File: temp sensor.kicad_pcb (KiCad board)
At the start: 2 copper layers, 48.2 x 24.9 mm, 52 parts, among them IC1 ESP32-C3-MINI-1, J1 USB_C_Receptacle_USB2.0, J2 Conn_01x02_Male, J3 Conn_01x06_Male, J4 USB_B_Micro, J5 Conn_01x02_Male, J6 Conn_01x02_Male, Q1 BC847BDW1, SW1 SW_Push_Right_Angle, SW2 SW_Push_Right_Angle, U1 SHTC3, U2 TLV62569DBV, U3 BME280, U4 Si7020-A20, U5 SN65220

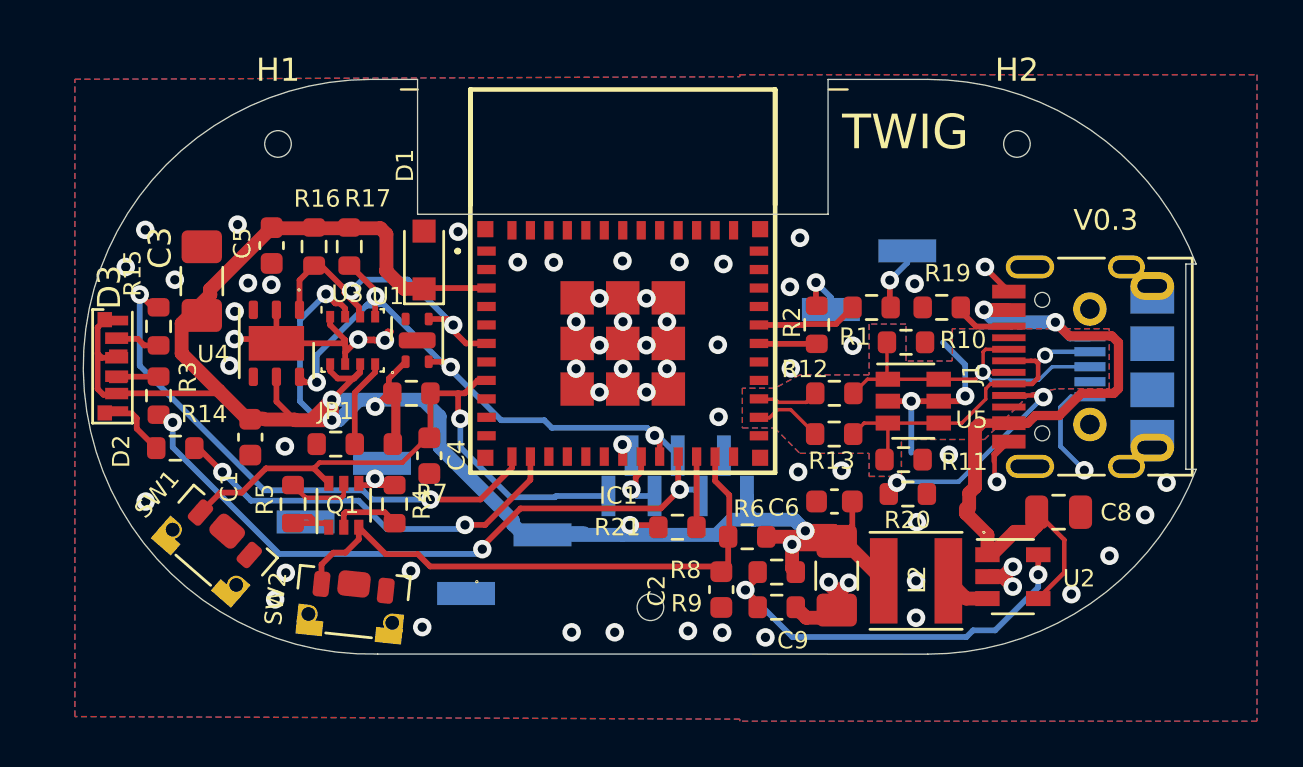
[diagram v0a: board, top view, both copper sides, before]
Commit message: added support for AS7341 and removed support for one of the temp/humidity sensors
Signed-off-by: lokimetasmith <lokimail@gmail.com>
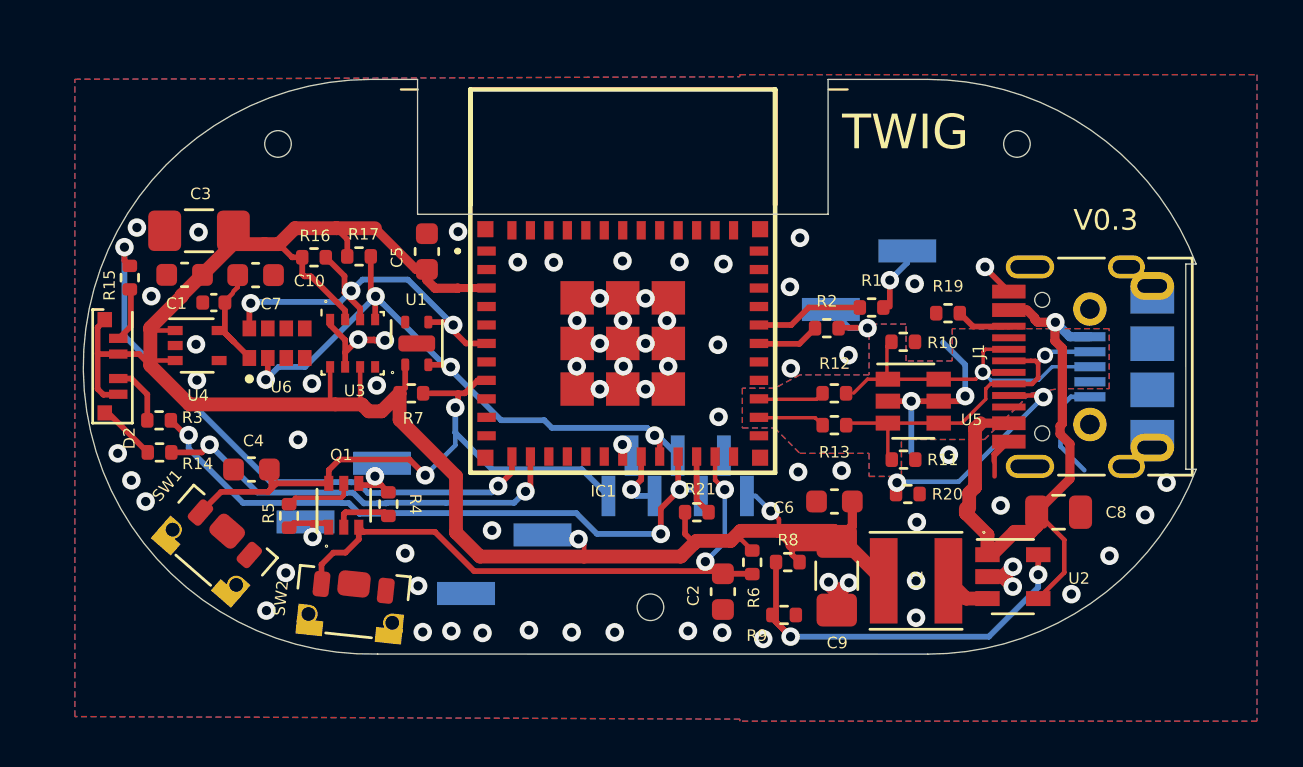
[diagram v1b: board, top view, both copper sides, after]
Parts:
- removed D1: 3.3v_TVS, Diode_SMD:D_SOD-323_HandSoldering
- removed D3: LED_GRB, Twig:99-235-RSGBB7C-A22-2D
- removed JP1: Jumper_3_Bridged12, Twig:Jumper_0603_1608Metric
- added C10: 0.1u, Capacitor_SMD:C_0603_1608Metric, F.Cu at (124.4, 88.7)
- added C7: 1u, Capacitor_SMD:C_0402_1005Metric, F.Cu at (122.6, 89.9)
- added U6: AS7341-DLGT, Twig:PSON80P310X200X110-8N, F.Cu at (125.4, 91.6)
- R1, R10, R11, R12, R13, R14, R15, R16, R17, R19, R2, R20, R21, R3, R4, R5, R6, R7, R8, R9: footprint Resistor_SMD:R_0603_1608Metric -> Resistor_SMD:R_0402_1005Metric
- U4: value Si7020-A20 -> MIC5365-3.3YC5; footprint Package_DFN_QFN:DFN-6-1EP_3x3mm_P1mm_EP1.5x2.4mm -> Package_TO_SOT_SMD:SOT-353_SC-70-5
- moved C4 7.73 mm to (124.2, 97.1), turned to 0 degrees
- moved C1 7.58 mm to (121.4, 88.7), turned to 180 degrees
- moved C5 6.73 mm to (131.8, 87.7), turned to 90 degrees
- moved U4 3.43 mm to (121.9, 91.7), turned to 0 degrees
- moved R15 2.45 mm to (119.0, 88.8)
- moved C3 2.18 mm to (122.0, 86.8), turned to 180 degrees
- moved R6 1.13 mm to (145.9, 101.1), turned to 90 degrees
- moved R3 1.07 mm to (120.2, 95.0), turned to 180 degrees
- moved R21 1.06 mm to (143.5, 99.0)
- moved R14 0.71 mm to (120.3, 96.4)
- moved R8 0.65 mm to (147.5, 101.1)
- moved R17 0.60 mm to (128.9, 87.9), turned to 180 degrees
- moved R5 0.54 mm to (125.9, 99.1)
- moved R16 0.47 mm to (127.0, 87.9), turned to 180 degrees
- moved R9 0.46 mm to (147.3, 103.4)
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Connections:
- U3 pad 5: Net-(JP1-Pad2) -> GND
- U4 pad 1: /I38_pico -> +3V3
- U4 pad 3: unconnected-(U4-Pad3) -> +3V3
- U4 pad 5: +3V3 -> +1V8
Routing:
- net GND: track 37.2 -> 28.6 mm, vias 66 -> 70
- net +3V3: track 100.1 -> 92.8 mm, vias 7 -> 2
- net +1V8: track 0.00 -> 5.03 mm
- net Net-(JP1-Pad2): track 3.83 -> 0.00 mm
- net /I38_pico: track 13.9 -> 17.7 mm, vias 2 -> 3
- net /V_USB: track 31.9 -> 28.5 mm, vias 2 -> 1
- net /Boot_Option: track 25.2 -> 28.5 mm, vias 0 -> 2
- net /EN: track 26.0 -> 28.0 mm, vias 1 -> 2
- net /IO32_pico: track 23.5 -> 25.4 mm
- net /RK: track 1.61 -> 2.66 mm
- net /IO15_pico: track 29.4 -> 28.4 mm
- net /IO13_pico: track 27.1 -> 28.1 mm
- net /RTX0: track 2.41 -> 3.19 mm
- net /IO33_pico: track 17.7 -> 18.3 mm
- net /GK: track 3.11 -> 2.56 mm
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
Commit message: added cutout model, minor changes to pcb
Signed-off-by: lokimetasmith <lokimail@gmail.com>
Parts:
- added SYM1: SYM_Arrow_Normal, Twig:Sensor Keepout block, F.Cu at (132.6, 92.7)
- C1, C10, C2, C4, C5, C6: footprint Capacitor_SMD:C_0603_1608Metric -> Capacitor_SMD:C_0402_1005Metric
- C7: footprint Capacitor_SMD:C_0402_1005Metric -> Capacitor_SMD:C_0603_1608Metric
- moved C7 2.24 mm to (124.5, 88.7), turned to 0 degrees
- moved C10 2.07 mm to (122.7, 89.9), turned to 180 degrees
- moved C1 0.91 mm to (120.4, 88.6)
- moved R7 0.31 mm to (131.2, 94.1)
- moved U2 0.17 mm to (157.4, 101.6)
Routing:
- net GND: track 28.6 -> 26.1 mm, vias 70 -> 82
- net /V_USB: track 28.5 -> 27.7 mm
- net +3V3: track 92.8 -> 93.5 mm

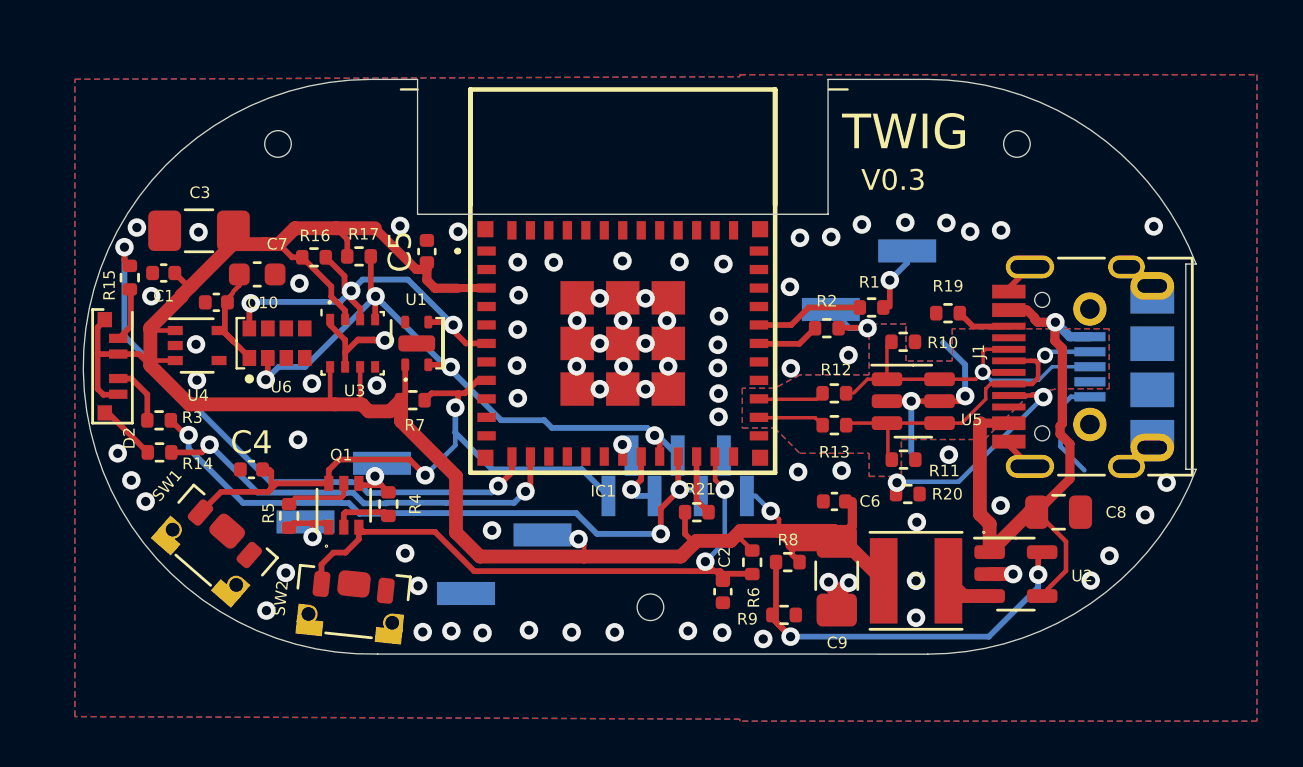
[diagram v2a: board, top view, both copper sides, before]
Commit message: added led cutout block
Signed-off-by: lokimetasmith <lokimail@gmail.com>
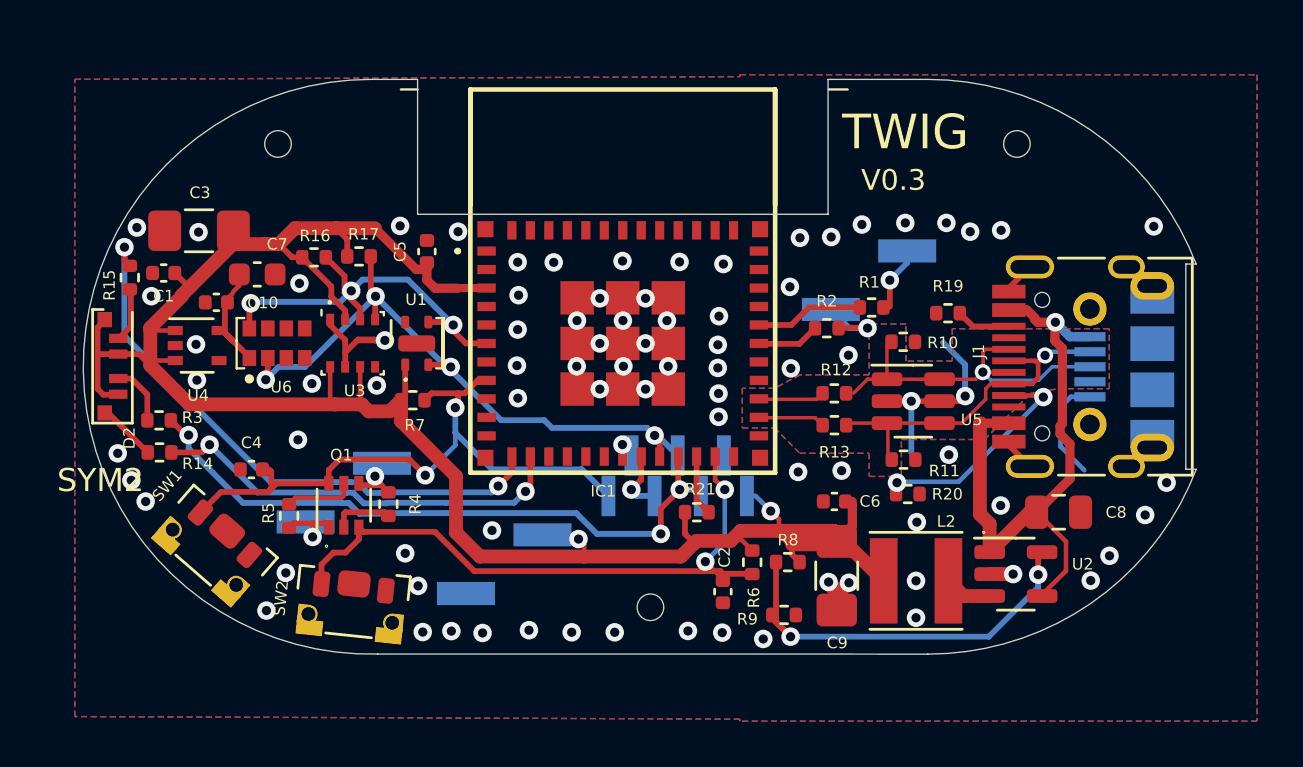
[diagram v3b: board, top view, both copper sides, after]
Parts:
- added SYM2: SYM_Arrow_Normal, Twig:LED Keepout block, F.Cu at (117.6, 95.2)
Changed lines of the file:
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@@
       (plotinvisibletext false)
       (sketchpadsonfab false)
-      (subtractmaskfromsilk false)
+      (subtractmaskfromsilk true)
       (outputformat 1)
       (mirror false)
@@
     (property "Sheetname" "")
     (attr smd)
-    (fp_text reference "L2" (at -0.04518 0.05684 90) (layer "F.SilkS")
+    (fp_text reference "L2" (at -1.305 2.571 180) (layer "F.SilkS")
       (effects (font (size 0.5 0.5) (thickness 0.1)))
     )
@@
     (property "Sheetname" "")
     (attr smd)
-    (fp_text reference "U2" (at 2.86512 0.07874) (layer "F.SilkS")
+    (fp_text reference "U2" (at 2.89 -0.43) (layer "F.SilkS")
       (effects (font (size 0.5 0.5) (thickness 0.1)))
     )
@@
     (attr smd)
     (fp_text reference "C4" (at 0 -1.16) (layer "F.SilkS")
-      (effects (font (size 1 1) (thickness 0.15)))
+      (effects (font (size 0.5 0.5) (thickness 0.1)))
     )
     (fp_text value "0.1u" (at 0 1.16) (layer "F.Fab")
@@
     (attr smd)
     (fp_text reference "C5" (at 0 -1.16 90) (layer "F.SilkS")
-      (effects (font (size 1 1) (thickness 0.15)))
+      (effects (font (size 0.5 0.5) (thickness 0.1)))
     )
     (fp_text value "0.1u" (at 0 1.16 90) (layer "F.Fab")
@@
     )
   )
+  (footprint "Twig:LED Keepout block" (layer "F.Cu")
+    (at 117.618 95.2)
+    (property "Sheetfile" "temp sensor.kicad_sch")
+    (property "Sheetname" "")
+    (fp_text reference "SYM2" (at 0.09 2.37 unlocked) (layer "F.SilkS")
+      (effects (font (size 1 1) (thickness 0.1)))
+    )
+    (fp_text value "SYM_Arrow_Normal" (at 0 1 unlocked) (layer "F.Fab")
+      (effects (font (size 1 1) (thickness 0.15)))
+    )
+    (fp_rect (start 0 0) (end -1.08 -5.1) (layer "Dwgs.User") (width 0.1) (fill none))
+    (model "${KIPRJMOD}/overmolding/Unnamed1-led_window_cutout001 (Solid).step"
+      (offset (xyz 0 0 0))
+      (scale (xyz 1 1 1))
+      (rotate (xyz 0 0 -90))
+    )
+  )
   (footprint "Package_TO_SOT_SMD:SOT-353_SC-70-5" (layer "F.Cu")
     (at 121.898 91.73)
@@
     (effects (font (size 1 1) (thickness 0.15)))
   )
-  (dimension (type aligned) (layer "F.Cu")
-    (pts (xy 132.573 92.72) (xy 132.578 90.54))
-    (height 37.916322)
-    (gr_text "2.1800 mm" (at 168.691727 91.712836 89.86858789) (layer "F.Cu")
-      (effects (font (size 1.5 1.5) (thickness 0.3)))
-    )
-    (format (units 3) (units_format 1) (precision 4))
-    (style (thickness 0.2) (arrow_length 1.27) (text_position_mode 0) (extension_height 0.58642) (extension_offset 0.5) keep_text_aligned)
-  )
   (dimension (type aligned) (layer "Dwgs.User")
     (pts (xy 165.25 92.51) (xy 116.96 92.51))
@@
     (style (thickness 0.15) (arrow_length 1.27) (text_position_mode 0) (extension_height 0.58642) (extension_offset 0) keep_text_aligned)
   )
+  (dimension (type aligned) (layer "Dwgs.User")
+    (pts (xy 132.573 92.72) (xy 132.578 90.54))
+    (height 37.916322)
+    (gr_text "2.1800 mm" (at 168.691727 91.712836 89.86858789) (layer "Dwgs.User")
+      (effects (font (size 1.5 1.5) (thickness 0.3)))
+    )
+    (format (units 3) (units_format 1) (precision 4))
+    (style (thickness 0.2) (arrow_length 1.27) (text_position_mode 0) (extension_height 0.58642) (extension_offset 0.5) keep_text_aligned)
+  )
   (segment (start 130.154886 91.381114) (end 130.028995 91.507005) (width 0.25) (layer "F.Cu") (net 1))
   (segment (start 149.75332 102.3784) (end 150.12744 102.00428) (width 0.6) (layer "F.Cu") (net 1))
@@
   (via (at 144.498 90.46) (size 0.8) (drill 0.4) (layers "F.Cu" "B.Cu") (free) (net 1))
   (via (at 144.6385 104.16582) (size 0.8) (drill 0.4) (layers "F.Cu" "B.Cu") (net 1))
-  (via (at 152.568 86.4) (size 0.8) (drill 0.4) (layers "F.Cu" "B.Cu") (free) (net 1))
+  (via (at 152.568 86.42) (size 0.8) (drill 0.4) (layers "F.Cu" "B.Cu") (free) (net 1))
   (via (at 150.688 86.49) (size 0.8) (drill 0.4) (layers "F.Cu" "B.Cu") (free) (net 1))
   (via (at 118.458 96.4) (size 0.8) (drill 0.4) (layers "F.Cu" "B.Cu") (free) (net 1))

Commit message: cribbed schematic corrections from https://github.com/esp-rs/esp-rust-board/tree/master/hardware/esp-rust-board
tweaked part layout, added back in zener 3v3 diode, added filter diode, and made minor tweaks.

Signed-off-by: lokimetasmith <lokimail@gmail.com>
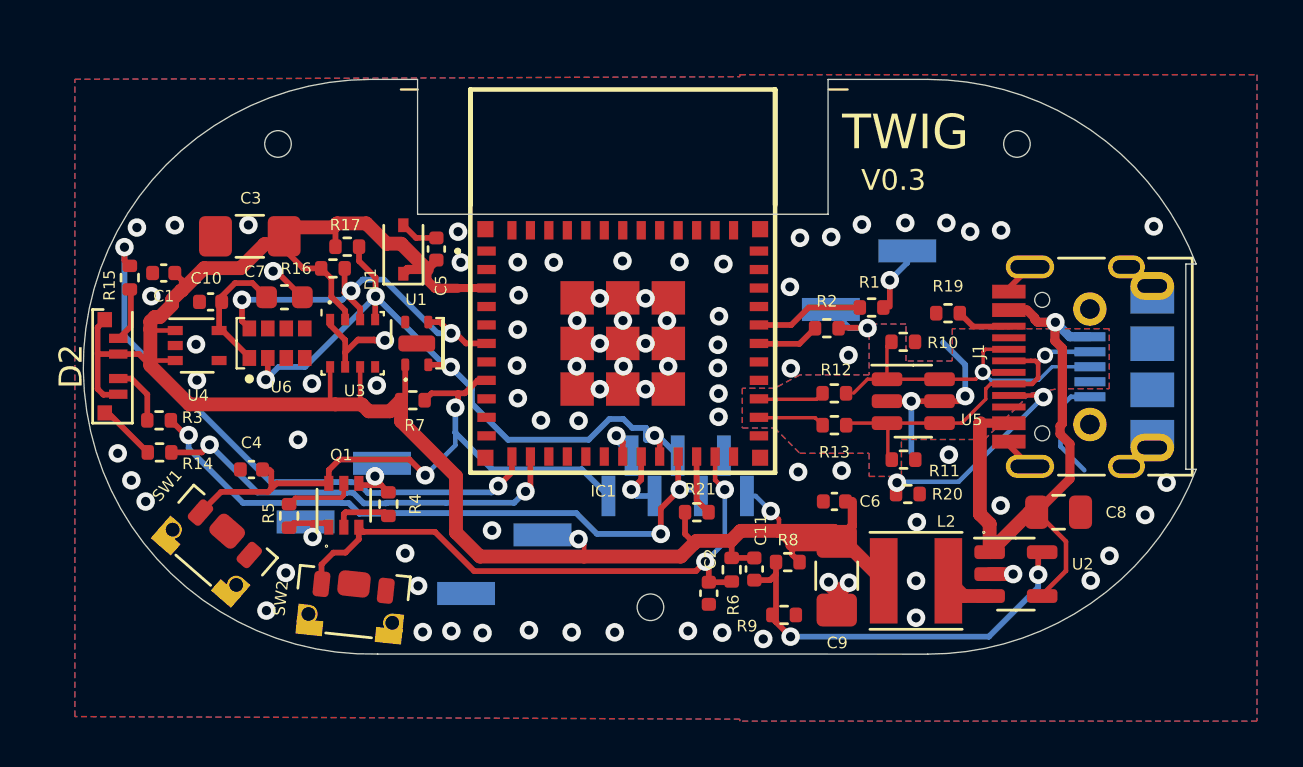
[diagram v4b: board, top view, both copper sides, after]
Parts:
- added C11: 6.8p, Capacitor_SMD:C_0402_1005Metric, F.Cu at (146.0, 101.4)
- added D1: 3.3v_TVS, Diode_SMD:D_SOD-323, F.Cu at (130.8, 87.6)
- D2: footprint LED_SMD:LED_Cree-PLCC6_4.7x1.5mm -> Twig:LED_Cree-PLCC6_4.7x1.5mm
- moved C3 2.21 mm to (124.2, 87.0)
- moved C7 1.54 mm to (125.7, 89.6)
- moved R16 0.95 mm to (127.8, 88.4)
- moved R6 0.95 mm to (145.0, 101.4)
- moved R17 0.66 mm to (128.4, 87.5)
- moved C2 0.61 mm to (144.1, 102.5)
- moved C5 0.42 mm to (132.3, 87.5)
- moved C10 0.25 mm to (122.5, 89.8)
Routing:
- net GND: track 26.1 -> 29.2 mm, vias 82 -> 85
- net +3V3: track 93.5 -> 95.9 mm
- net /IO13_pico: track 28.1 -> 30.2 mm
- net /Boot_Option: track 28.5 -> 26.4 mm
- net /IO14_pico: track 1.16 -> 2.15 mm
